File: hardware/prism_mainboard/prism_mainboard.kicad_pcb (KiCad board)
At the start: 2 copper layers, 1 part, among them U1 XC7Z010-1CLG400C

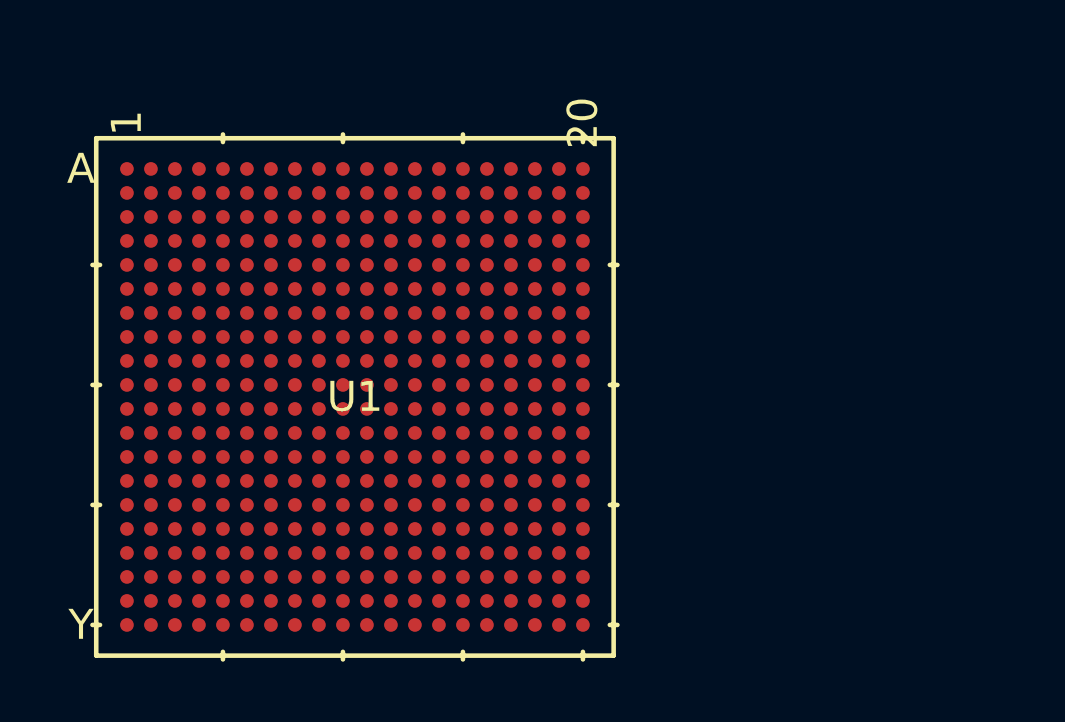
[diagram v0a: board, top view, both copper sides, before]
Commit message: KiCAD Update
Added Power System Schematics. Decided on a 4 in 1 Buck and LDO, LP87222TQ1, for 3.3V and 1.8V LDO, and 1.8V and 1.0V Buck converter.
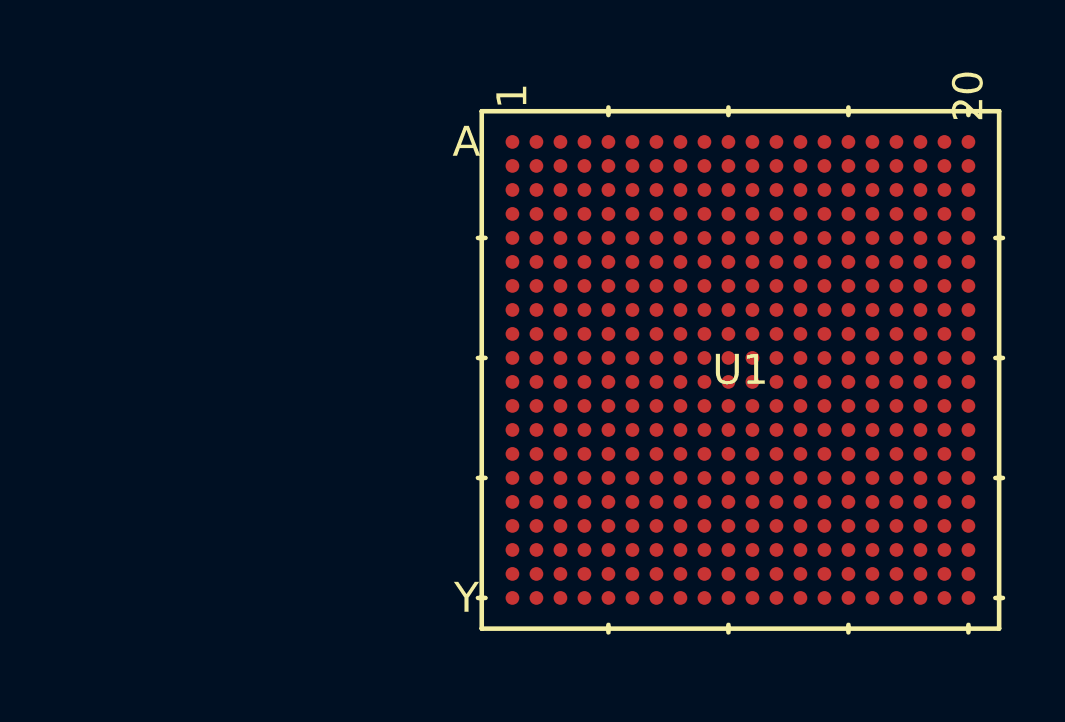
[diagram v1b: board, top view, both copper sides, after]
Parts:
- moved U1 12.9 mm to (105.2, 86.2)

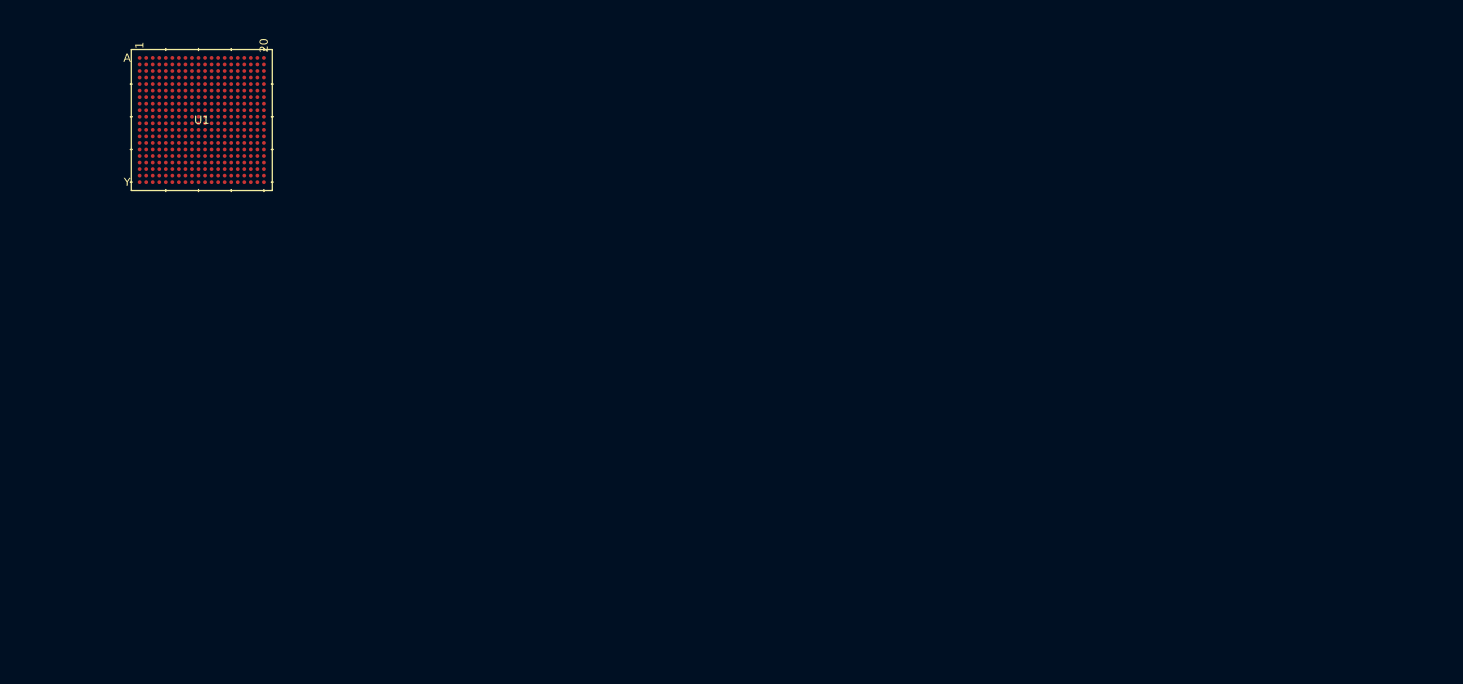
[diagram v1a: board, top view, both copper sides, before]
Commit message: Schematics
More schematics updates, moving to Desktop for editing. Continued with power usage, debating use of Dedicated DDR3/3L power IC instead of using LDO and Buck from mainboard power.
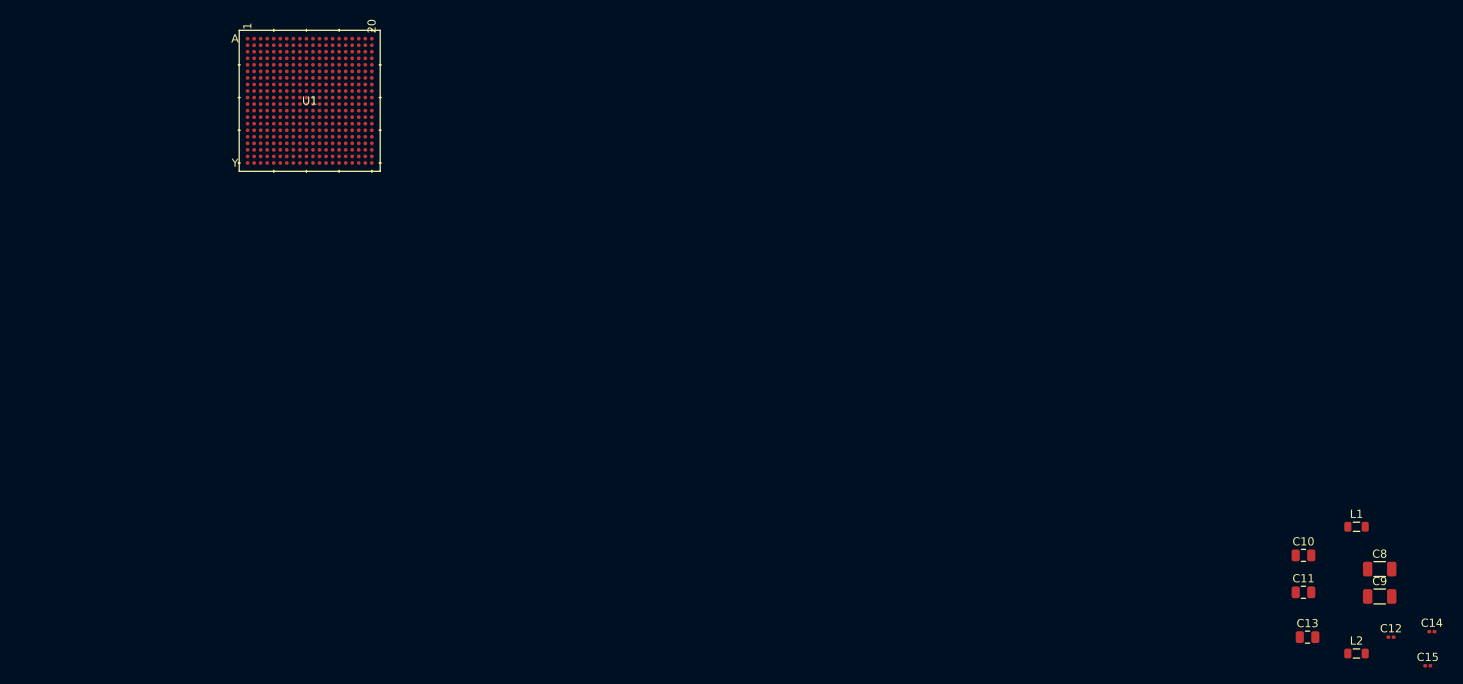
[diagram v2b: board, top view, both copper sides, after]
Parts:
- added C10: 10uF, Capacitor_SMD:C_0805_2012Metric, F.Cu at (239.9, 139.5)
- added C11: 4.7uF, Capacitor_SMD:C_0805_2012Metric, F.Cu at (239.9, 144.0)
- added C12: 2.2uF, Capacitor_SMD:C_0201_0603Metric, F.Cu at (250.7, 149.5)
- added C13: 10uF, Capacitor_SMD:C_0805_2012Metric, F.Cu at (240.4, 149.5)
- added C14: 1uF, Capacitor_SMD:C_0201_0603Metric, F.Cu at (255.7, 148.8)
- added C15: 2.2uF, Capacitor_SMD:C_0201_0603Metric, F.Cu at (255.2, 153.0)
- added C8: 22uF, Capacitor_SMD:C_1206_3216Metric, F.Cu at (249.3, 141.2)
- added C9: 22uF, Capacitor_SMD:C_1206_3216Metric, F.Cu at (249.3, 144.5)
- added L1: 0.47uH, Inductor_SMD:L_0805_2012Metric, F.Cu at (246.4, 136.0)
- added L2: 0.47uH, Inductor_SMD:L_0805_2012Metric, F.Cu at (246.4, 151.5)
- moved U1 13.4 mm to (118.4, 83.9)
